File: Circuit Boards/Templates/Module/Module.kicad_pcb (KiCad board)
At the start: 2 copper layers, 220 x 100 mm, 2 parts, among them P1 DIN41612-C-96-M-RA

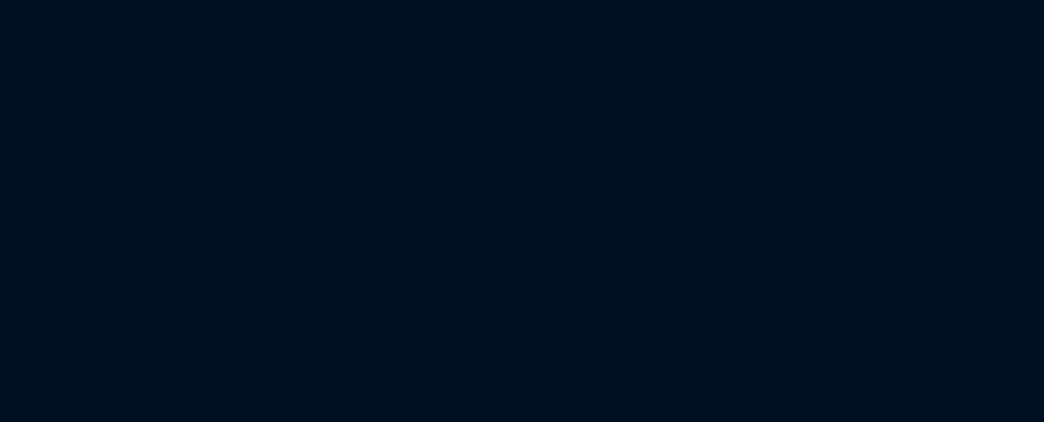
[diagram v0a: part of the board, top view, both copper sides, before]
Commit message: Backplane: Initial PCB layout
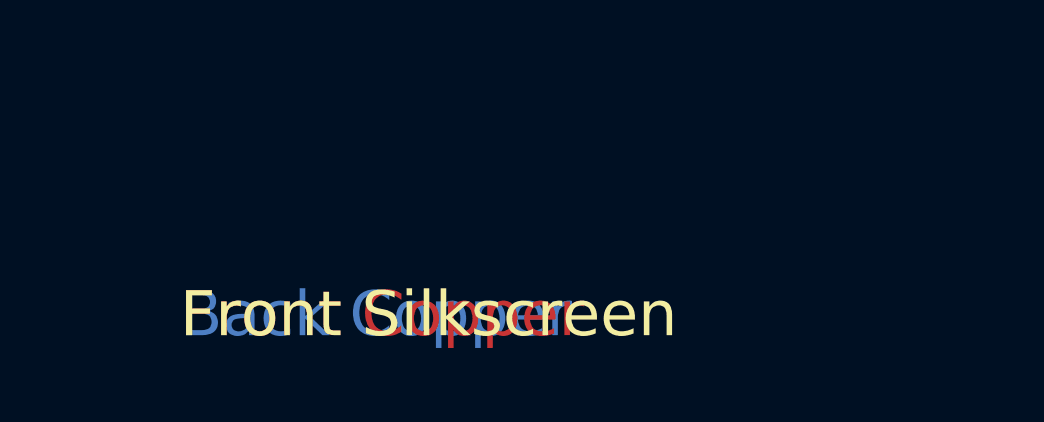
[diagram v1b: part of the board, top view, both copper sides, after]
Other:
- board text added: "Back Copper"
- board text added: "Back Silkscreen"
- board text added: "Front Copper"
- board text added: "Front Silkscreen"
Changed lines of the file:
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@@
     )
+  )
+  (gr_text "Back Silkscreen" (at 198.628 198.628) (layer B.SilkS)
+    (effects (font (size 1.5 1.5) (thickness 0.15)) (justify left))
+  )
+  (gr_text "Front Silkscreen" (at 198.628 198.628) (layer F.SilkS)
+    (effects (font (size 1.5 1.5) (thickness 0.15)) (justify left))
+  )
+  (gr_text "Back Copper" (at 198.628 198.628) (layer B.Cu)
+    (effects (font (size 1.5 1.5) (thickness 0.15)) (justify left))
+  )
+  (gr_text "Front Copper" (at 198.628 198.628) (layer F.Cu)
+    (effects (font (size 1.5 1.5) (thickness 0.15)) (justify left))
   )
   (gr_line (start 38.7 55) (end 258.3 55) (angle 90) (layer Edge.Cuts) (width 0.1))
